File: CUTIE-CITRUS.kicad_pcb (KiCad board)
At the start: 4 copper layers, 78.5 x 78.5 mm, 82 parts, among them J1 F32Q-1A7H1-11022, J2 F32Q-1A7H1-11022, J3 Bus_M.2_Socket_M, P1 ERM8-025-01-L-D-RA-K-TR, U1 AP3441SHE-7B, U3 ICM-42688-P, U5 MCP98243, U6 MCP98243, U7 MCP2518FD-xQBB, U8 TCAN334, Y1 ECS-2520MV-200-BN-TR, Y2 ASEK-32.768KHZ-L-R-T

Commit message: tp and gnd vias fixes
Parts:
- moved TP11 7.50 mm to (127.5, 110.0)
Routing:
- net GND: vias 324 -> 329
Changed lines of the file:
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@@
 		(tags "test point SMD pad")
 		(property "Reference" "TP14"
-			(at 0.9 -1.55 0)
+			(at 1.05 -1.5 0)
 			(layer "B.SilkS")
 			(effects
@@
 		(tags "test point SMD pad")
 		(property "Reference" "TP13"
-			(at 0.8 1.45 0)
+			(at 1.1 1.4 0)
 			(layer "B.SilkS")
 			(effects
@@
 		(tags "test point SMD pad")
 		(property "Reference" "TP12"
-			(at 0 -1.5 0)
+			(at 0 -1.45 0)
 			(layer "B.SilkS")
 			(effects
@@
 	(footprint "TestPoint:TestPoint_Pad_D1.0mm"
 		(layer "B.Cu")
-		(at 135 110 180)
+		(at 127.5 110 180)
 		(descr "SMD pad as test Point, diameter 1.0mm")
 		(tags "test point SMD pad")
 		(property "Reference" "TP11"
-			(at 0 -1.55 0)
+			(at 0 -1.45 0)
 			(layer "B.SilkS")
 			(effects
@@
 	)
 	(via
-		(at 135.25 126.5)
+		(at 134.95 126.8)
 		(size 0.5)
 		(drill 0.25)
 		(layers "F.Cu" "B.Cu")
-		(locked yes)
 		(free yes)
 		(net 4)
@@
 	)
 	(via
-		(at 133 126.5)
+		(at 132.2 126.5)
 		(size 0.5)
 		(drill 0.25)
 		(layers "F.Cu" "B.Cu")
-		(locked yes)
 		(free yes)
 		(net 4)
@@
 	)
 	(via
+		(at 126.25 134.5)
+		(size 0.61)
+		(drill 0.3)
+		(layers "F.Cu" "B.Cu")
+		(free yes)
+		(net 4)
+	)
+	(via
 		(at 156.5 126.25)
 		(size 0.4064)
@@
 	)
 	(via
-		(at 130 121.75)
+		(at 129.45 122.65)
 		(size 0.5)
 		(drill 0.25)
 		(layers "F.Cu" "B.Cu")
-		(locked yes)
 		(free yes)
 		(net 4)
@@
 	)
 	(via
+		(at 130 134.5)
+		(size 0.61)
+		(drill 0.3)
+		(layers "F.Cu" "B.Cu")
+		(free yes)
+		(net 4)
+	)
+	(via
 		(at 136.15 102.75)
 		(size 0.5)
@@
 	)
 	(via
+		(at 131.25 134.5)
+		(size 0.61)
+		(drill 0.3)
+		(layers "F.Cu" "B.Cu")
+		(free yes)
+		(net 4)
+	)
+	(via
 		(at 131.25 58)
 		(size 0.61)
@@
 	)
 	(via
+		(at 128.75 134.5)
+		(size 0.61)
+		(drill 0.3)
+		(layers "F.Cu" "B.Cu")
+		(free yes)
+		(net 4)
+	)
+	(via
 		(at 137.5 85)
 		(size 0.5)
@@
 	)
 	(via
+		(at 127.5 134.5)
+		(size 0.61)
+		(drill 0.3)
+		(layers "F.Cu" "B.Cu")
+		(free yes)
+		(net 4)
+	)
+	(via
 		(at 162.5 130)
 		(size 0.5)
@@
 		(drill 0.25)
 		(layers "F.Cu" "B.Cu")
-		(locked yes)
 		(net 70)
 	)
@@
 		(polygon
 			(pts
-				(xy 161.45 64.45) (xy 124.597368 64.45) (xy 124.8 91.4) (xy 131.8 91.4) (xy 131.8 70) (xy 139.6 70)
-				(xy 161.45 70)
+				(xy 161.45 64) (xy 124.593985 64) (xy 124.8 91.4) (xy 131.8 91.4) (xy 131.8 70) (xy 139.6 70) (xy 161.45 70)
 			)
 		)

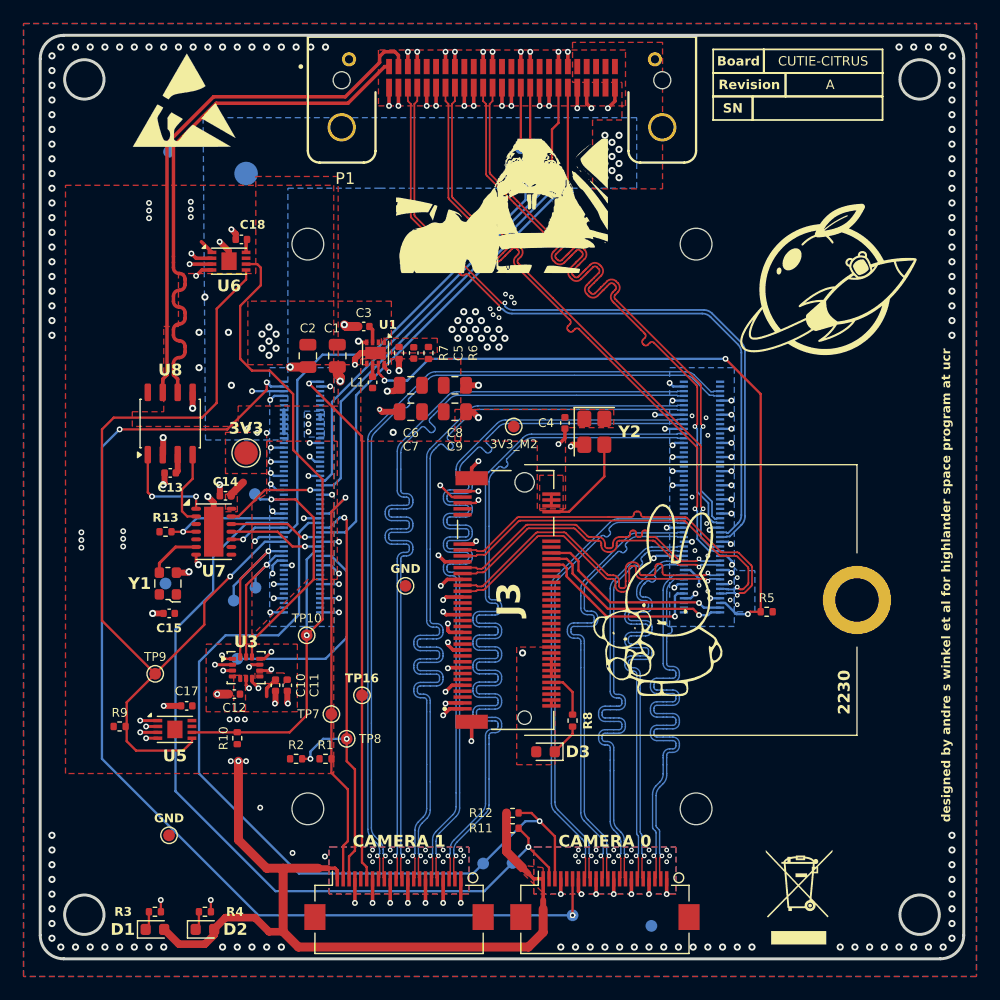
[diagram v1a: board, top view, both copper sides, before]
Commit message: redid gpio layout, removed one temp sensor, bom
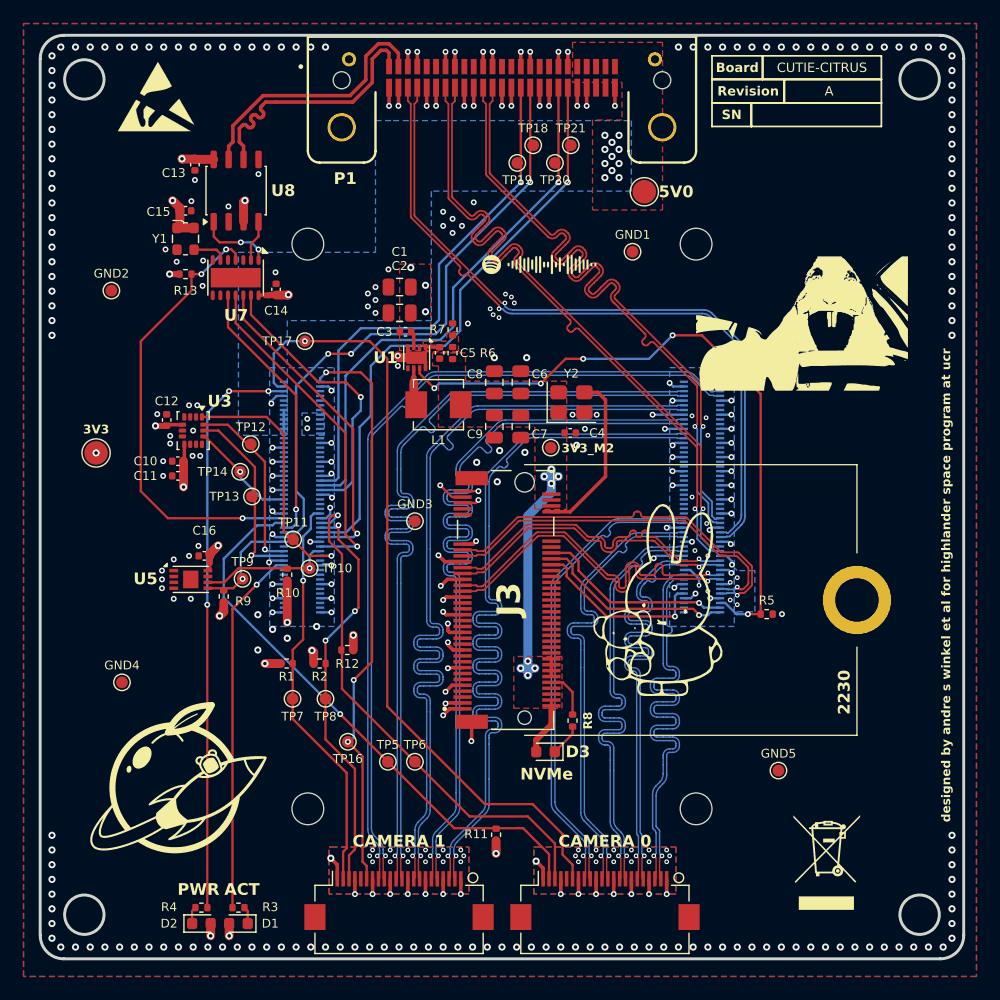
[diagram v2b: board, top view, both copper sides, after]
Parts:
- removed C17, C18: 0.1uF, Capacitor_SMD:C_0402_1005Metric
- removed the G*** at (150.0, 101.2)
- removed GND (x5): TestPoint, TestPoint:TestPoint_Pad_D1.0mm
- removed the REF** at (123.0, 62.5)
- removed U6: MCP98243, Package_DFN_QFN:DFN-8-1EP_3x2mm_P0.5mm_EP1.3x1.5mm
- added C16: 0.1uF, Capacitor_SMD:C_0402_1005Metric, F.Cu at (124.7, 101.2)
- added G***: LOGO, LOGO, B.Cu at (150.0, 98.3)
- added G***: LOGO, LOGO, F.Cu at (153.2, 76.5)
- added G***: LOGO, LOGO, B.Cu at (116.7, 74.4)
- added GND1: TestPoint, TestPoint:TestPoint_Pad_D1.0mm, F.Cu at (161.1, 75.4)
- added GND2: TestPoint, TestPoint:TestPoint_Pad_D1.0mm, F.Cu at (116.8, 78.7)
- added GND3: TestPoint, TestPoint:TestPoint_Pad_D1.0mm, F.Cu at (142.6, 98.3)
- added GND4: TestPoint, TestPoint:TestPoint_Pad_D1.0mm, F.Cu at (117.7, 112.0)
- added GND5: TestPoint, TestPoint:TestPoint_Pad_D1.0mm, F.Cu at (173.5, 119.5)
- added REF**: ESD-Logo_6.6x6mm_SilkScreen, Symbol:ESD-Logo_6.6x6mm_SilkScreen, F.Cu at (120.6, 62.2)
- 5V0, TP11, TP12, TP13, TP14, TP17, TP18, TP19, TP20, TP21, TP5, TP6: moved to F.Cu
- D3: value LED Green -> LED Blue
- J3: value Bus_M.2_Socket_M -> SM3ZS067U410ABR1000
- L1: footprint Capacitor_SMD:C_0402_1005Metric -> Inductor_SMD:L_Vishay_IHLP-1616
- R8: value 1K -> 1k
- moved G*** 70.7 mm to (179.5, 119.0)
- moved G*** 69.6 mm to (122.5, 120.1)
- moved G*** 58.2 mm to (121.3, 117.0)
- moved TP17 53.8 mm to (133.2, 83.0), turned to 0 degrees
- moved C15 34.3 mm to (123.1, 71.9), turned to 0 degrees
- moved 5V0 33.9 mm to (162.1, 70.3), turned to 0 degrees
- moved Y1 29.3 mm to (123.1, 74.3), turned to 0 degrees
- moved G*** 27.4 mm to (175.5, 81.5)
- moved C13 26.3 mm to (123.9, 68.0), turned to -90 degrees
- moved C12 24.0 mm to (121.5, 89.7), turned to 90 degrees
- moved R13 22.0 mm to (123.1, 77.3)
- moved U7 21.7 mm to (127.4, 77.6), turned to -90 degrees
- moved C10 20.8 mm to (122.5, 93.2), turned to 180 degrees
- moved U3 20.6 mm to (123.8, 90.6), turned to -90 degrees
- moved U8 20.6 mm to (127.4, 70.2)
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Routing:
- net /CM5/I2C2.SDA: track 75.6 -> 9.63 mm
- net GND: track 201.7 -> 138.6 mm, vias 329 -> 356
- net /CM5/I2C2.SCL: track 62.7 -> 11.3 mm
- net /CM5/3V3: track 77.4 -> 43.2 mm, vias 24 -> 26
- net /CM5/CAN_INT: track 11.1 -> 38.7 mm, vias 1 -> 3
- net /CM5/I2C0.SCL: track 70.6 -> 44.1 mm
- net /CM5/CAM0_EN: track 93.3 -> 67.3 mm, vias 3 -> 1
- net /Backplane Connector/CAN0.P: track 45.6 -> 22.6 mm
- net /Backplane Connector/CAN0.N: track 45.4 -> 22.5 mm
- net /CM5/GPIO/SPI3.MOSI: track 8.06 -> 28.8 mm
- net /CM5/I2C0.SDA: track 68.9 -> 48.5 mm
- net /CM5/GPIO/SPI3.MISO: track 8.00 -> 27.5 mm
- net /CM5/GPIO/SPI3.SCLK: track 4.88 -> 23.0 mm
- net /CM5/GPIO/SPI3.CS0n: track 8.47 -> 24.4 mm
- net /CM5/SPI1.CS0n: track 20.9 -> 9.28 mm
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- added copper zone on In2.Cu, net /CM5/3V3
- removed copper zone on F.Cu, net /CM5/3V3
- removed copper zone on In1.Cu, net /CM5/3V3
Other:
- board text added: "ACT"
- board text added: "NVMe"
- board text added: "PWR"
